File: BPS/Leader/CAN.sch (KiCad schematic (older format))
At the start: 19 parts, among them J9 CAN_Out, U10 ADM3055E, U11 CDSOT23-T24CAN

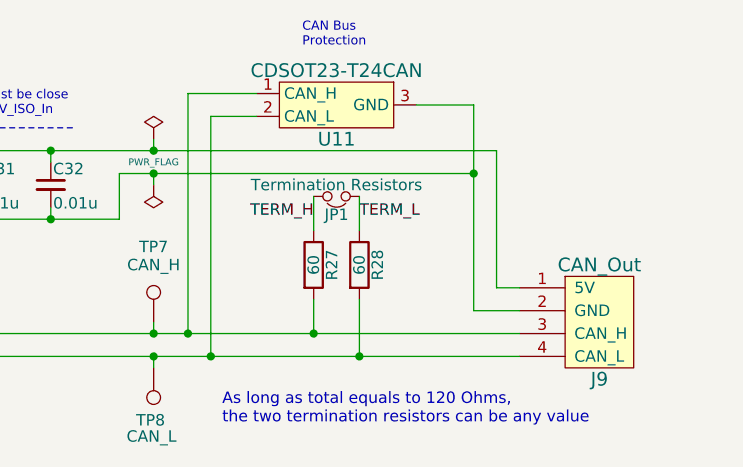
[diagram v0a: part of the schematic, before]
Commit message: Places most components of leader board in their respective locations with nothing traced
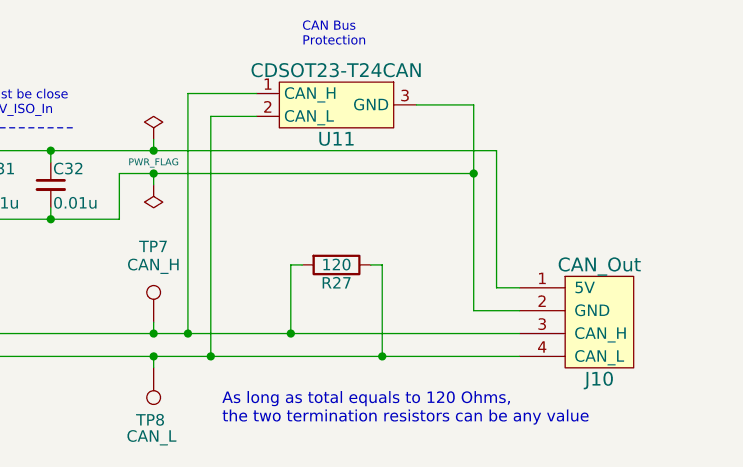
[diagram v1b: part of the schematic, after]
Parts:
- removed JP1: Termination Resistors, Connector_PinHeader_2.54mm:PinHeader_1x02_P2.54mm_Vertical, symbol Device:Jumper_NC_Small
- removed R28: 60, Resistor_SMD:R_0805_2012Metric, symbol Device:R
- R27: value 60 -> 120
- renumbered J9 to J10
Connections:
- net TERM_H is gone; now on net CAN_L: R27.1
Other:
- moved on the sheet: R27
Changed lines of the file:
@@
 $EndDescr
 $Comp
-L utsvt-connectors:CANConnector J9
+L utsvt-connectors:CANConnector J10
 U 1 1 5C2B42F3
 P 9250 3800
-F 0 "J9" H 9250 3550 60  0000 C CNN
+F 0 "J10" H 9250 3550 60  0000 C CNN
 F 1 "CAN_Out" H 9250 4050 60  0000 C CNN
 F 2 "UTSVT_Connectors:Molex_MicroFit3.0_1x4xP3.00mm_PolarizingPeg_Vertical" H 9400 4100 60  0001 C CNN
@@
 $EndComp
 $Comp
-L Device:R R28
-U 1 1 5C2B42FA
-P 8200 3550
-F 0 "R28" V 8280 3550 50  0000 C CNN
-F 1 "60" V 8200 3550 50  0000 C CNN
-F 2 "Resistor_SMD:R_0805_2012Metric" V 8130 3550 50  0001 C CNN
-F 3 "" H 8200 3550 50  0001 C CNN
-	1    8200 3550
-	1    0    0    -1
-$EndComp
-$Comp
 L Device:R R27
 U 1 1 5C2B4301
-P 8000 3550
-F 0 "R27" V 8080 3550 50  0000 C CNN
-F 1 "60" V 8000 3550 50  0000 C CNN
-F 2 "Resistor_SMD:R_0805_2012Metric" V 7930 3550 50  0001 C CNN
-F 3 "" H 8000 3550 50  0001 C CNN
-	1    8000 3550
-	1    0    0    -1
-$EndComp
-$Comp
-L Device:Jumper_NC_Small JP1
-U 1 1 5C2B4308
-P 8100 3250
-F 0 "JP1" H 8100 3330 50  0000 C CNN
-F 1 "Termination Resistors" H 8100 3200 50  0000 C CNN
-F 2 "Connector_PinHeader_2.54mm:PinHeader_1x02_P2.54mm_Vertical" H 8100 3250 50  0001 C CNN
-F 3 "" H 8100 3250 50  0001 C CNN
-	1    8100 3250
-	-1   0    0    1
+P 8100 3550
+F 0 "R27" V 8180 3550 50  0000 C CNN
+F 1 "120" V 8100 3550 50  0000 C CNN
+F 2 "Resistor_SMD:R_0805_2012Metric" V 8030 3550 50  0001 C CNN
+F 3 "" H 8100 3550 50  0001 C CNN
+	1    8100 3550
+	0    1    1    0
 $EndComp
 $Comp
@@
 NoConn ~ 3650 4100
 $Comp
-L power:PWR_FLAG #FLG03
+L power:PWR_FLAG #FLG07
 U 1 1 5C2B4394
 P 7300 3000
-F 0 "#FLG03" H 7300 3075 50  0001 C CNN
+F 0 "#FLG07" H 7300 3075 50  0001 C CNN
 F 1 "PWR_FLAG" H 7300 2900 30  0000 C CNN
 F 2 "" H 7300 3000 50  0001 C CNN
@@
 $EndComp
 $Comp
-L power:PWR_FLAG #FLG04
+L power:PWR_FLAG #FLG08
 U 1 1 5C2B439A
 P 7300 3200
-F 0 "#FLG04" H 7300 3275 50  0001 C CNN
+F 0 "#FLG08" H 7300 3275 50  0001 C CNN
 F 1 "PWR_FLAG" H 7200 3150 50  0001 L CNN
 F 2 "" H 7300 3200 50  0001 C CNN
@@
 Wire Notes Line
 	6500 2950 6950 2950
-Wire Wire Line
-	8000 3250 8000 3400
-Wire Wire Line
-	8200 3250 8200 3400
 Connection ~ 5250 3350
 Connection ~ 6150 3550
@@
 Wire Wire Line
 	7300 3050 7300 3000
-Wire Wire Line
-	8000 3850 8000 3700
-Wire Wire Line
-	8200 3950 8200 3700
 Wire Wire Line
 	7750 2900 7550 2900
@@
 Wire Wire Line
 	2950 3500 3300 3500
-Connection ~ 8000 3850
-Wire Wire Line
-	8000 3850 8900 3850
-Connection ~ 8200 3950
-Wire Wire Line
-	8200 3950 8900 3950
-Wire Wire Line
-	7450 3850 8000 3850
-Wire Wire Line
-	7550 3950 8200 3950
 Wire Wire Line
 	7150 3150 7300 3150
@@
 Text Label 5050 3950 0    50   ~ 0
 CAN_L
-Text Label 8000 3350 2    50   ~ 0
-TERM_H
-Text Label 8200 3350 0    50   ~ 0
-TERM_L
 Connection ~ 5750 3050
 Wire Wire Line
@@
 Text Notes 7600 4250 0    50   ~ 0
 As long as total equals to 120 Ohms,\nthe two termination resistors can be any value
+Wire Wire Line
+	7450 3850 7900 3850
+Wire Wire Line
+	7550 3950 8300 3950
+Wire Wire Line
+	7950 3550 7900 3550
+Wire Wire Line
+	7900 3550 7900 3850
+Connection ~ 7900 3850
+Wire Wire Line
+	7900 3850 8900 3850
+Wire Wire Line
+	8250 3550 8300 3550
+Wire Wire Line
+	8300 3550 8300 3950
+Connection ~ 8300 3950
+Wire Wire Line
+	8300 3950 8900 3950
 $EndSCHEMATC

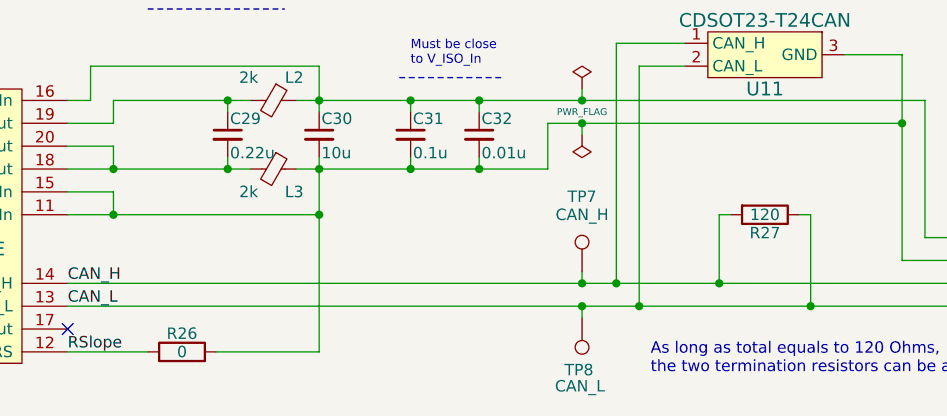
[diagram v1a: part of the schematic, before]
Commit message: Adds power planes
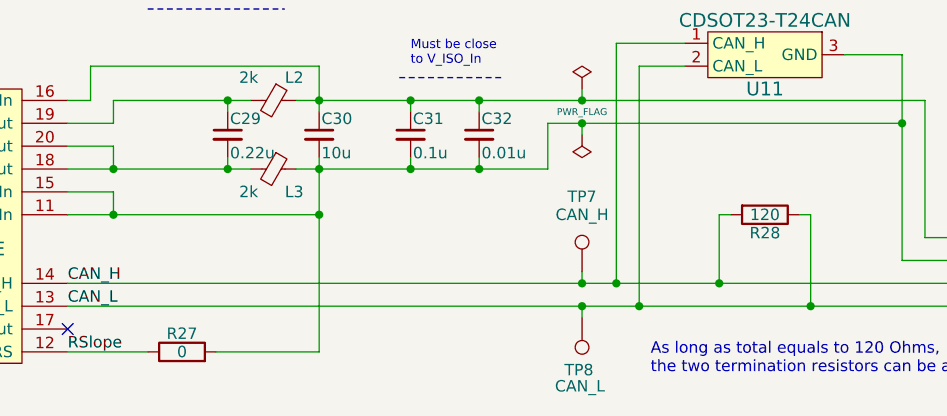
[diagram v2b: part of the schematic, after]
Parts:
- renumbered R26 to R27, R27 to R28
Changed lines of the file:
@@
 $EndComp
 $Comp
-L Device:R R27
+L Device:R R28
 U 1 1 5C2B4301
 P 8100 3550
-F 0 "R27" V 8180 3550 50  0000 C CNN
+F 0 "R28" V 8180 3550 50  0000 C CNN
 F 1 "120" V 8100 3550 50  0000 C CNN
 F 2 "Resistor_SMD:R_0805_2012Metric" V 8030 3550 50  0001 C CNN
@@
 $EndComp
 $Comp
-L Device:R R26
+L Device:R R27
 U 1 1 5C2B43C4
 P 5550 4150
-F 0 "R26" V 5630 4150 50  0000 C CNN
+F 0 "R27" V 5630 4150 50  0000 C CNN
 F 1 "0" V 5550 4150 50  0000 C CNN
 F 2 "Resistor_SMD:R_0805_2012Metric" V 5480 4150 50  0001 C CNN

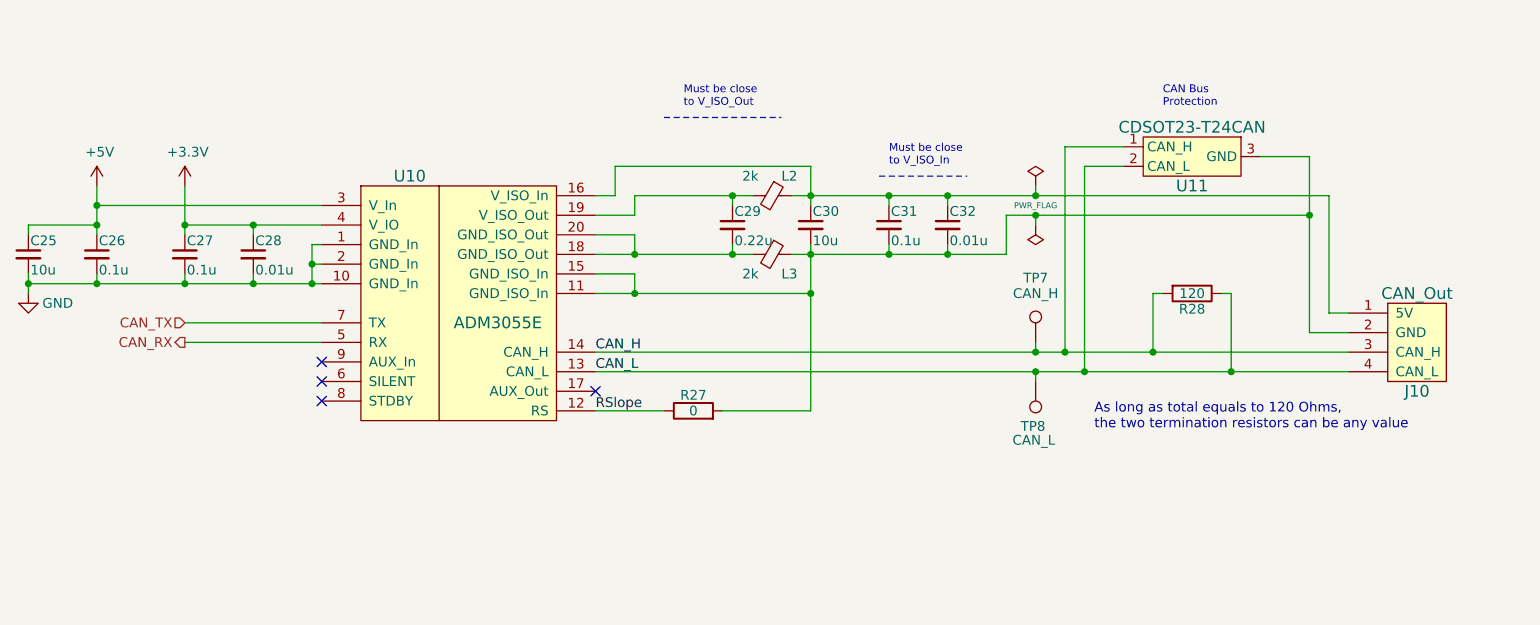
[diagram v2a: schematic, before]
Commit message: Finished leader board
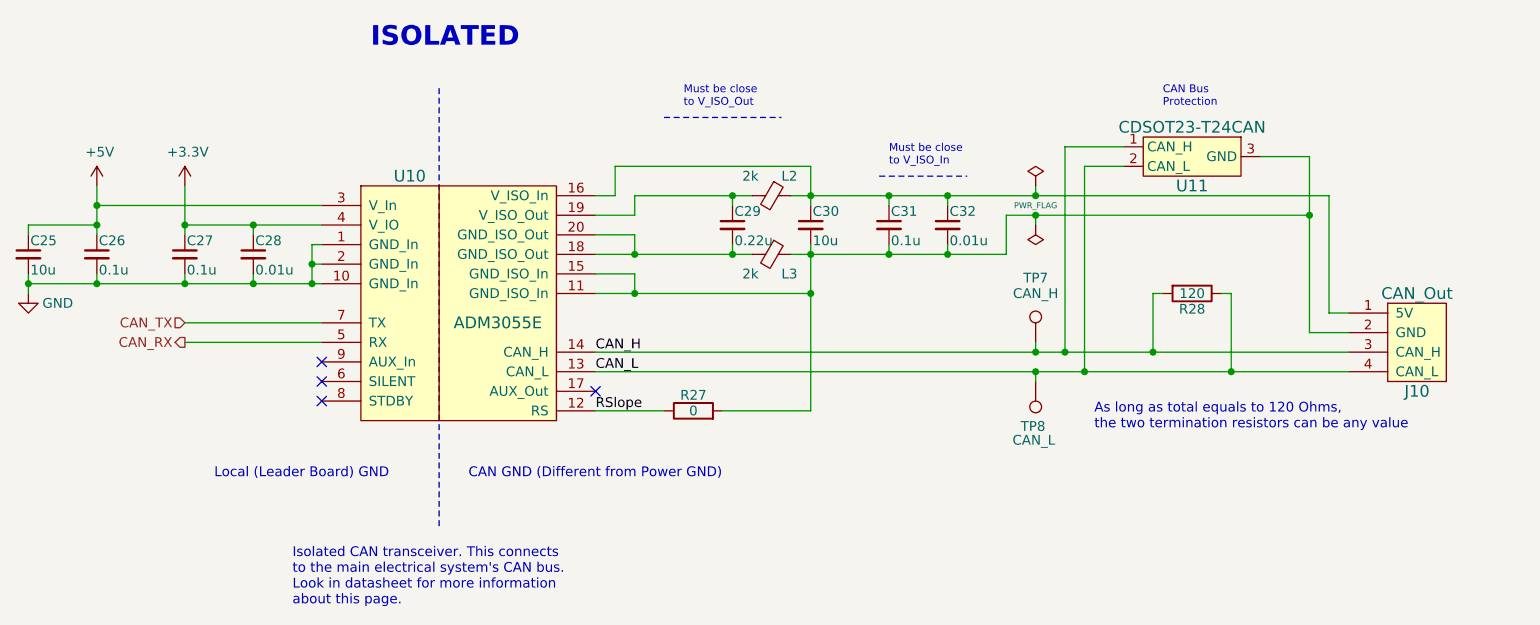
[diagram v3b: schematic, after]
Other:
- note added: "CAN GND (Different from Power GND)"
- note added: "ISOLATED"
- note added: "Isolated CAN transceiver. This connects\nto the main electrical system's CAN bus.\nLook in datasheet for more information\nabout this page."
- note added: "Local (Leader Board) GND"
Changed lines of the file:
@@
 Wire Wire Line
 	8300 3950 8900 3950
+Wire Notes Line
+	4250 2500 4250 4750
+Text Notes 3900 2300 0    100  ~ 20
+ISOLATED
+Text Notes 3100 4500 0    50   ~ 0
+Local (Leader Board) GND
+Text Notes 4400 4500 0    50   ~ 0
+CAN GND (Different from Power GND)
+Text Notes 3500 5150 0    50   ~ 0
+Isolated CAN transceiver. This connects\nto the main electrical system's CAN bus.\nLook in datasheet for more information\nabout this page.
 $EndSCHEMATC

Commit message: Simplifies dc-dc converter schematics
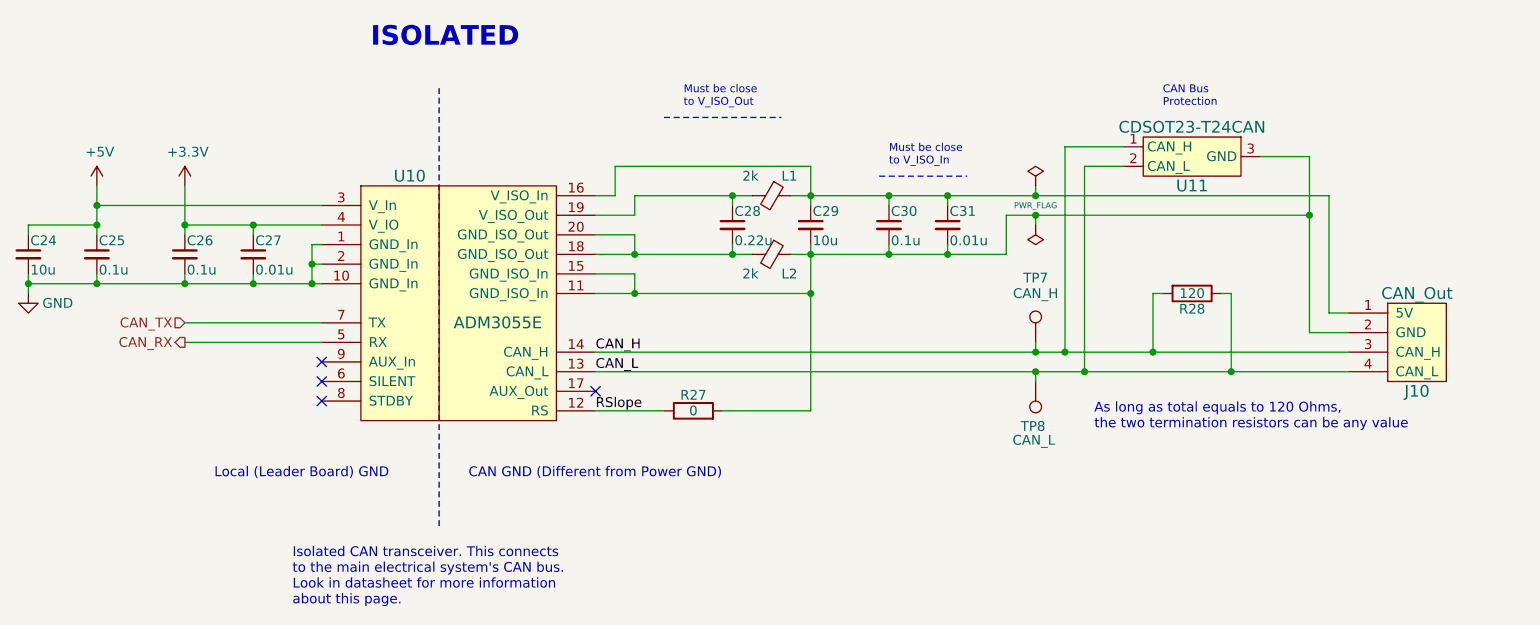
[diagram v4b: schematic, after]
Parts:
- renumbered C25 to C24, C26 to C25, C27 to C26, C28 to C27, C29 to C28, C30 to C29, C31 to C30, C32 to C31, L2 to L1, L3 to L2
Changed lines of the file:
@@
 $EndComp
 $Comp
-L Device:C_Small C25
+L Device:C_Small C24
 U 1 1 5C2B4310
 P 2150 3350
-F 0 "C25" H 2160 3420 50  0000 L CNN
+F 0 "C24" H 2160 3420 50  0000 L CNN
 F 1 "10u" H 2160 3270 50  0000 L CNN
 F 2 "Capacitor_SMD:C_0805_2012Metric" H 2150 3350 50  0001 C CNN
@@
 $EndComp
 $Comp
-L Device:C_Small C26
+L Device:C_Small C25
 U 1 1 5C2B4317
 P 2500 3350
-F 0 "C26" H 2510 3420 50  0000 L CNN
+F 0 "C25" H 2510 3420 50  0000 L CNN
 F 1 "0.1u" H 2510 3270 50  0000 L CNN
 F 2 "Capacitor_SMD:C_0805_2012Metric" H 2500 3350 50  0001 C CNN
@@
 $EndComp
 $Comp
-L Device:C_Small C27
+L Device:C_Small C26
 U 1 1 5C2B431E
 P 2950 3350
-F 0 "C27" H 2960 3420 50  0000 L CNN
+F 0 "C26" H 2960 3420 50  0000 L CNN
 F 1 "0.1u" H 2960 3270 50  0000 L CNN
 F 2 "Capacitor_SMD:C_0805_2012Metric" H 2950 3350 50  0001 C CNN
@@
 $EndComp
 $Comp
-L Device:C_Small C28
+L Device:C_Small C27
 U 1 1 5C2B4325
 P 3300 3350
-F 0 "C28" H 3310 3420 50  0000 L CNN
+F 0 "C27" H 3310 3420 50  0000 L CNN
 F 1 "0.01u" H 3310 3270 50  0000 L CNN
 F 2 "Capacitor_SMD:C_0805_2012Metric" H 3300 3350 50  0001 C CNN
@@
 $EndComp
 $Comp
-L Device:C_Small C30
+L Device:C_Small C29
 U 1 1 5C2B432E
 P 6150 3200
-F 0 "C30" H 6160 3270 50  0000 L CNN
+F 0 "C29" H 6160 3270 50  0000 L CNN
 F 1 "10u" H 6160 3120 50  0000 L CNN
 F 2 "Capacitor_SMD:C_0805_2012Metric" H 6150 3200 50  0001 C CNN
@@
 $EndComp
 $Comp
-L Device:C_Small C29
+L Device:C_Small C28
 U 1 1 5C2B4335
 P 5750 3200
-F 0 "C29" H 5760 3270 50  0000 L CNN
+F 0 "C28" H 5760 3270 50  0000 L CNN
 F 1 "0.22u" H 5760 3120 50  0000 L CNN
 F 2 "Capacitor_SMD:C_0805_2012Metric" H 5750 3200 50  0001 C CNN
@@
 $EndComp
 $Comp
-L Device:Ferrite_Bead_Small L2
+L Device:Ferrite_Bead_Small L1
 U 1 1 5C2B433C
 P 5950 3050
-F 0 "L2" V 5850 3100 50  0000 L CNN
+F 0 "L1" V 5850 3100 50  0000 L CNN
 F 1 "2k" V 5850 2900 50  0000 L CNN
 F 2 "Inductor_SMD:L_0805_2012Metric" V 5880 3050 50  0001 C CNN
@@
 $EndComp
 $Comp
-L Device:Ferrite_Bead_Small L3
+L Device:Ferrite_Bead_Small L2
 U 1 1 5C2B4343
 P 5950 3350
-F 0 "L3" V 6050 3400 50  0000 L CNN
+F 0 "L2" V 6050 3400 50  0000 L CNN
 F 1 "2k" V 6050 3200 50  0000 L CNN
 F 2 "Inductor_SMD:L_0805_2012Metric" V 5880 3350 50  0001 C CNN
@@
 $EndComp
 $Comp
-L Device:C_Small C31
+L Device:C_Small C30
 U 1 1 5C2B434A
 P 6550 3200
-F 0 "C31" H 6560 3270 50  0000 L CNN
+F 0 "C30" H 6560 3270 50  0000 L CNN
 F 1 "0.1u" H 6560 3120 50  0000 L CNN
 F 2 "Capacitor_SMD:C_0805_2012Metric" H 6550 3200 50  0001 C CNN
@@
 $EndComp
 $Comp
-L Device:C_Small C32
+L Device:C_Small C31
 U 1 1 5C2B4351
 P 6850 3200
-F 0 "C32" H 6860 3270 50  0000 L CNN
+F 0 "C31" H 6860 3270 50  0000 L CNN
 F 1 "0.01u" H 6860 3120 50  0000 L CNN
 F 2 "Capacitor_SMD:C_0805_2012Metric" H 6850 3200 50  0001 C CNN
@@
 NoConn ~ 3650 4100
 $Comp
-L power:PWR_FLAG #FLG07
+L power:PWR_FLAG #FLG06
 U 1 1 5C2B4394
 P 7300 3000
-F 0 "#FLG07" H 7300 3075 50  0001 C CNN
+F 0 "#FLG06" H 7300 3075 50  0001 C CNN
 F 1 "PWR_FLAG" H 7300 2900 30  0000 C CNN
 F 2 "" H 7300 3000 50  0001 C CNN
@@
 $EndComp
 $Comp
-L power:PWR_FLAG #FLG08
+L power:PWR_FLAG #FLG07
 U 1 1 5C2B439A
 P 7300 3200
-F 0 "#FLG08" H 7300 3275 50  0001 C CNN
+F 0 "#FLG07" H 7300 3275 50  0001 C CNN
 F 1 "PWR_FLAG" H 7200 3150 50  0001 L CNN
 F 2 "" H 7300 3200 50  0001 C CNN
@@
 	5250 3050 5250 3150
 $Comp
-L power:GND #PWR063
+L power:GND #PWR062
 U 1 1 5C28BDDE
 P 2150 3550
-F 0 "#PWR063" H 2150 3300 50  0001 C CNN
+F 0 "#PWR062" H 2150 3300 50  0001 C CNN
 F 1 "GND" H 2300 3500 50  0000 C CNN
 F 2 "" H 2150 3550 50  0001 C CNN
@@
 	2500 3000 2500 3100
 $Comp
-L power:+3.3V #PWR065
+L power:+3.3V #PWR064
 U 1 1 5C4ABE05
 P 2950 3000
-F 0 "#PWR065" H 2950 2850 50  0001 C CNN
+F 0 "#PWR064" H 2950 2850 50  0001 C CNN
 F 1 "+3.3V" H 2965 3173 50  0000 C CNN
 F 2 "" H 2950 3000 50  0001 C CNN
@@
 	2950 3000 2950 3200
 $Comp
-L power:+5V #PWR064
+L power:+5V #PWR063
 U 1 1 5C4C2AB0
 P 2500 3000
-F 0 "#PWR064" H 2500 2850 50  0001 C CNN
+F 0 "#PWR063" H 2500 2850 50  0001 C CNN
 F 1 "+5V" H 2515 3173 50  0000 C CNN
 F 2 "" H 2500 3000 50  0001 C CNN
